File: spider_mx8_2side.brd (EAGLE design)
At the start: 16.9 x 49.8 mm, 6 parts, among them J1 AVR_SPI_PRG_6NS

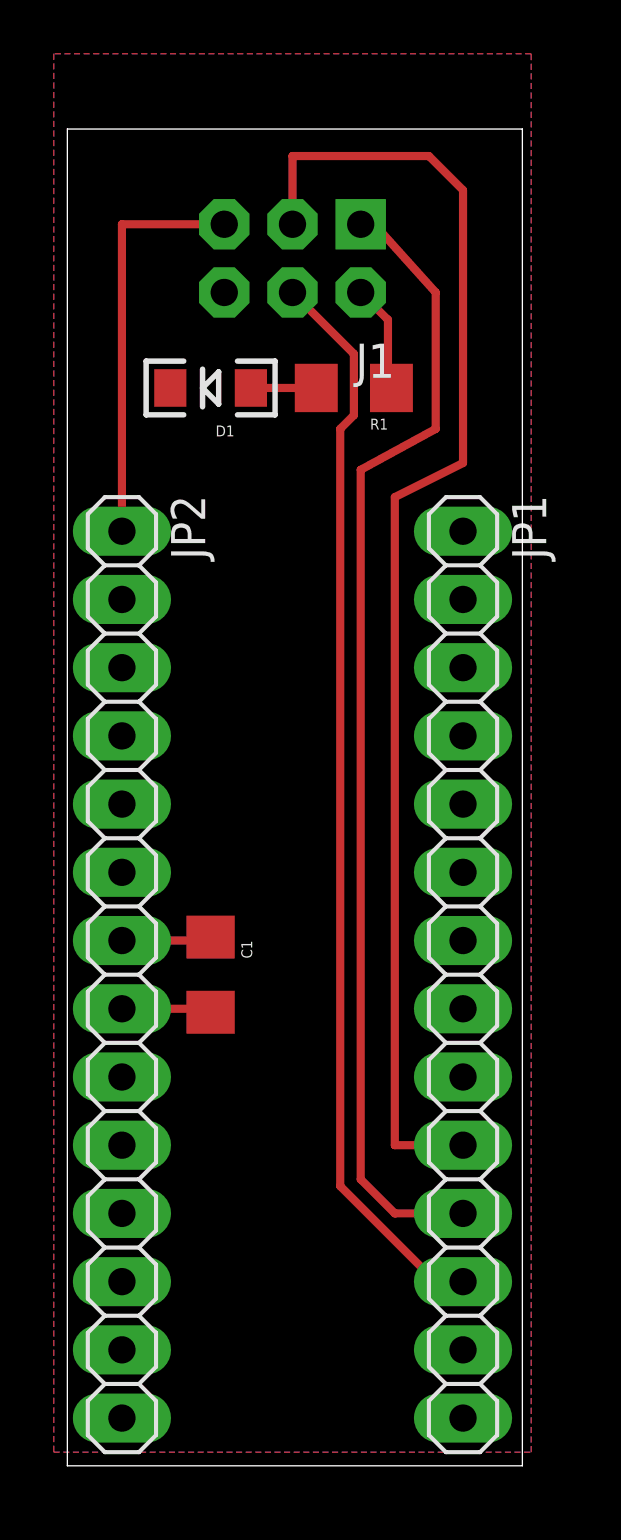
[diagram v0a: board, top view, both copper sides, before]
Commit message: untested, but probably good 2sided board
using thin pins.  need to check DRC for whatever foundry use
(esp the edge-routing may give trouble)
(also, the label layer on the bottom side.  think gold phoenix doesn't
do that.)
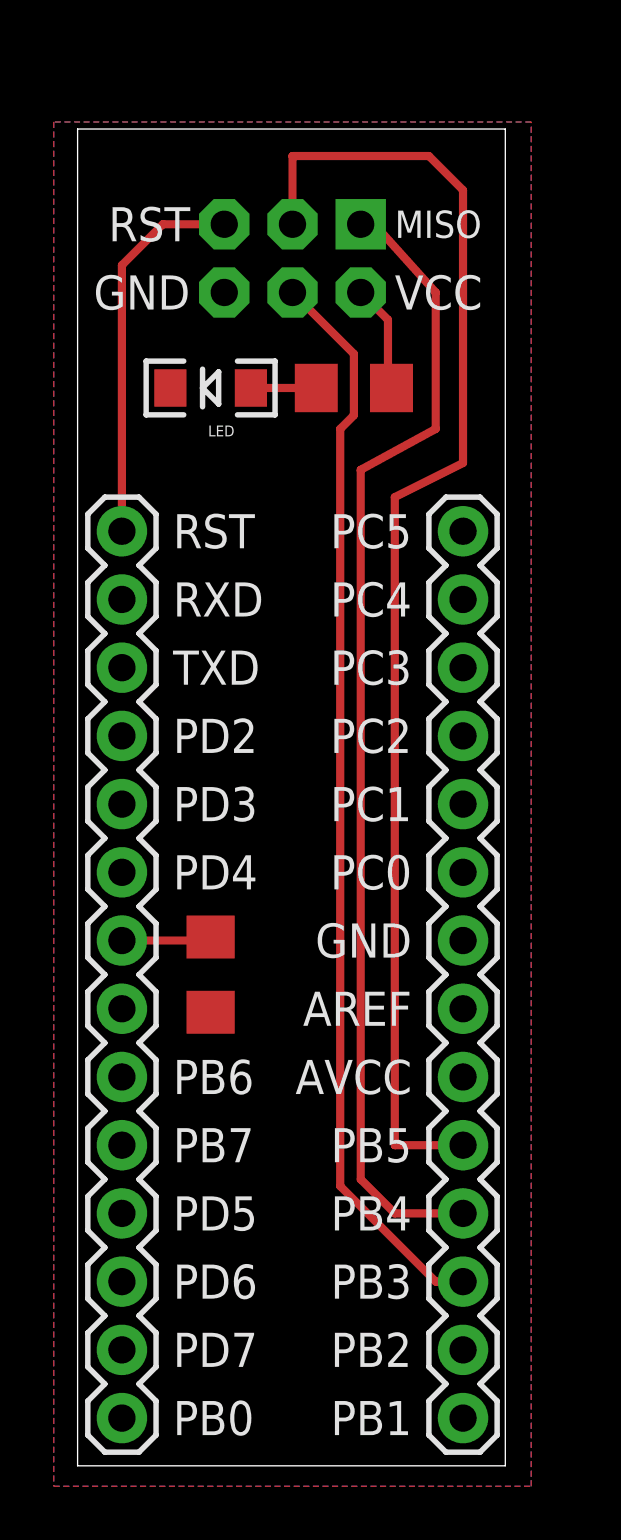
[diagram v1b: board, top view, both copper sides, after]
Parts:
- removed JP2: (no value), pinhead:1X14
- added JP3: M14, SparkFun-Connectors:1X14
- JP1: value (none) -> M14; device pinhead:1X14 -> SparkFun-Connectors:1X14
- moved JP1 20.8 mm to (36.8, 20.3), turned to 90 degrees
- renumbered D1 to LED
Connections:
- net GND: now also JP1.7; no longer JP2.8
- net MISO: now also JP3.11; no longer JP1.11
- net MOSI: now also JP3.12; no longer JP1.12
- net RESET: now also JP1.14; no longer JP2.1
- net SCK: now also JP3.10; no longer JP1.10
- net VCC: now also JP1.8; no longer JP2.7
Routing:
- net GND: track 3.43 -> 0.13 mm
- net RESET: track 15.2 -> 14.3 mm
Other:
- board size 16.9 x 49.8 mm -> 15.9 x 49.8 mm
- board text added: "AREF"
- board text added: "AVCC"
- board text added: "GND"
- board text added: "MISO"
- board text added: "Mega xx8 Programming Spider Version 1.0"
- board text added: "PB0"
- board text added: "PB1"
- board text added: "PB2"
- board text added: "PB3"
- board text added: "PB4"
- board text added: "PB5"
- board text added: "PB6"
- board text added: "PB7"
- board text added: "PC0"
- board text added: "PC1"
- board text added: "PC2"
- board text added: "PC3"
- board text added: "PC4"
- board text added: "PC5"
- board text added: "PD2"
- board text added: "PD3"
- board text added: "PD4"
- board text added: "PD5"
- board text added: "PD6"
- board text added: "PD7"
- board text added: "RST"
- board text added: "RXD"
- board text added: "TXD"
- board text added: "VCC"
